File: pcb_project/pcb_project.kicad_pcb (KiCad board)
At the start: 6 copper layers, 238 parts, among them IC1 TPS54325PWPR, IC2 TPS54294PWPR, IC3 IS61WV204816BLL-10TLI, IC4 IS61WV204816BLL-10TLI, J1 Conn_01x10_Pin, J10 M20-9990246, J11 M20-9990246, J12 M20-9990246, J2 FTSH-107-01-F-DV-K, J3 Conn_ST_STDC14, J4 DE15_Socket_HighDensity_Mount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, J5 USB_B_Micro, J6 MEM2052-00-195-00-A, J7 USB_A, J8 M20-9990246, J9 M20-9990246, Q1 BC857BS, Q2 BC847BPN, SW2 SW_SPDT, SW3 SW_SPST, SW4 SW_SPST, U1 XC7A100T-FTG256, U10 TPD1E1B04DPYT, U11 TPD1E1B04DPYT, U12 TPD1E1B04DPYT, U13 TPD1E1B04DPYT, U2 STM32U595VJTx, U3 TPS2041B, U4 D3V3XA4B10LP, U5 TPD1E1B04DPYT, U6 TPD1E1B04DPYT, U7 MAX7221xWG, U8 COM-11405, U9 MT25QL128ABA1ESE-0SIT, Y1 48MHz, Y2 XLH736025.175000I

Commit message: MicroSD layout, TVS issues
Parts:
- moved R59 59.6 mm to (125.4, 62.0), turned to 45 degrees
- moved R60 59.6 mm to (123.4, 60.0), turned to 45 degrees
- moved R61 59.6 mm to (121.4, 58.0), turned to 45 degrees
- moved R62 59.6 mm to (119.4, 56.0), turned to 45 degrees
- moved R63 59.6 mm to (117.4, 54.0), turned to 45 degrees
- moved R64 59.6 mm to (115.4, 52.0), turned to 45 degrees
- moved C77 56.1 mm to (172.9, 25.7)
- moved D11 56.1 mm to (167.0, 26.2)
- moved SW3 56.1 mm to (163.8, 30.9)
- moved SW2 56.1 mm to (153.2, 23.5)
- moved U11 28.7 mm to (110.0, 38.0), turned to -45 degrees
- moved U10 25.8 mm to (112.8, 33.8), turned to -45 degrees
- moved U6 23.9 mm to (115.4, 36.6), turned to -45 degrees
- moved U5 22.3 mm to (116.4, 30.4), turned to -45 degrees
- moved U13 20.1 mm to (119.6, 33.6), turned to -45 degrees
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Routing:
- net Net-(J6-DAT0): track 1.76 -> 72.1 mm, vias 1 -> 4
- net Net-(J6-DAT1): track 1.80 -> 65.8 mm, vias 1 -> 4
- net Net-(J6-DAT2): track 13.2 -> 61.7 mm, vias 1 -> 4
- net Net-(J6-CD/DAT3): track 12.0 -> 56.2 mm, vias 1 -> 4
- net /MCU/PB4_LPGPIO1_P12: track 0.00 -> 42.0 mm
- net Net-(J6-CMD): track 11.4 -> 48.8 mm, vias 1 -> 3
- net Net-(J6-CLK): track 1.76 -> 38.9 mm, vias 1 -> 2
- net +3V3: track 17.6 -> 30.6 mm, vias 3 -> 11
- net GND: track 10.6 -> 0.01 mm
- net Net-(U2-PA13): track 0.00 -> 3.23 mm
- net /MCU/PC9_SDMMC1_D1: track 6.53 -> 5.69 mm

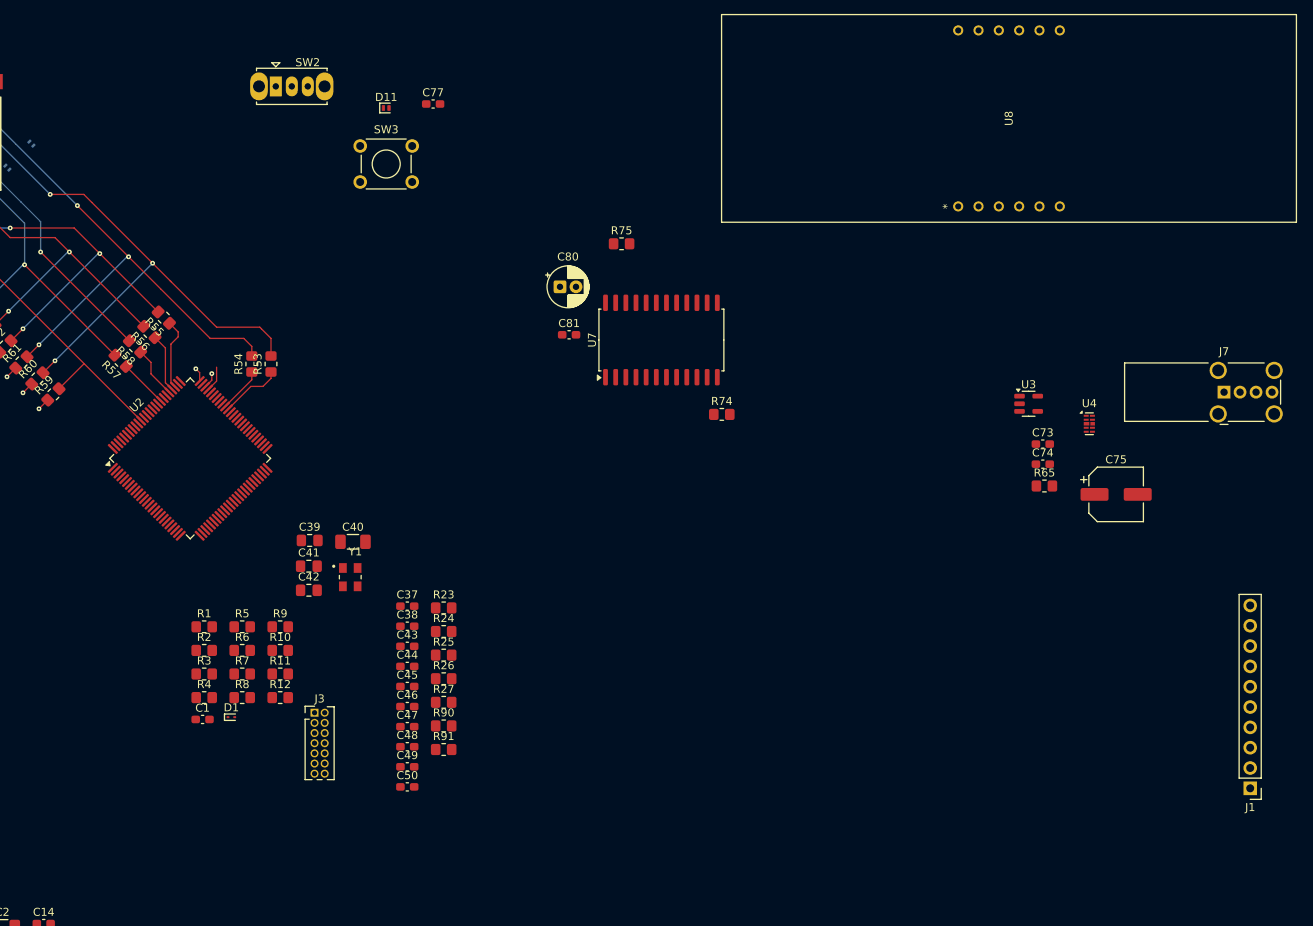
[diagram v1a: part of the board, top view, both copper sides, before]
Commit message: Layout MCU debug connector, reset and boot buttons
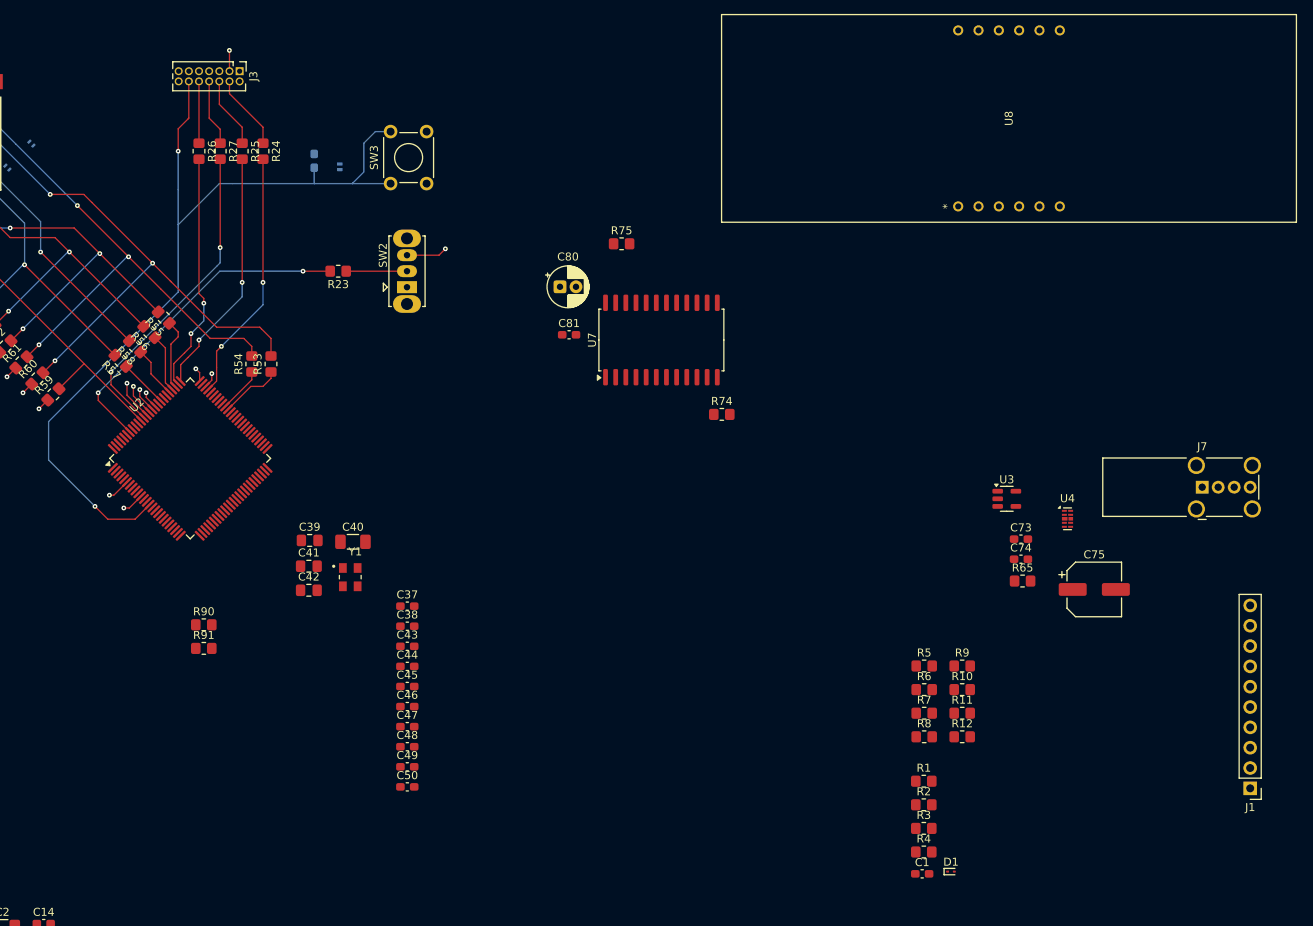
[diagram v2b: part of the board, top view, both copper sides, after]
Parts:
- C77, D11: moved to B.Cu
- moved C1 92.0 mm to (234.0, 121.9)
- moved D1 92.0 mm to (237.6, 121.7)
- moved R1 92.0 mm to (234.2, 110.3)
- moved R2 92.0 mm to (234.2, 113.3)
- moved R3 92.0 mm to (234.2, 116.2)
- moved R4 92.0 mm to (234.2, 119.2)
- moved R10 85.4 mm to (239.0, 98.9)
- moved R11 85.4 mm to (239.0, 101.8)
- moved R12 85.4 mm to (239.0, 104.8)
- moved R5 85.4 mm to (234.2, 96.0)
- moved R6 85.4 mm to (234.2, 98.9)
- moved R7 85.4 mm to (234.2, 101.8)
- moved R8 85.4 mm to (234.2, 104.8)
- moved R9 85.4 mm to (239.0, 96.0)
- moved J3 80.7 mm to (148.7, 21.6), turned to -90 degrees
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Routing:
- net Net-(D11-K): track 0.00 -> 111.3 mm, vias 0 -> 2
- net Net-(U2-PH3): track 0.00 -> 41.8 mm, vias 0 -> 2
- net Net-(U2-PB3): track 0.00 -> 39.7 mm, vias 0 -> 2
- net Net-(U2-PA14): track 0.00 -> 30.9 mm, vias 0 -> 2
- net Net-(U2-PA15): track 0.00 -> 30.1 mm, vias 0 -> 2
- net Net-(U2-PA13): track 3.23 -> 31.6 mm, vias 0 -> 2
- net +3V3: track 30.6 -> 44.0 mm, vias 11 -> 15
- net Net-(J3-JTMS/SWDIO): track 0.00 -> 9.47 mm
- net Net-(J3-JCLK/SWCLK): track 0.00 -> 8.91 mm
- net Net-(J3-JTDO/SWO): track 0.00 -> 8.30 mm
- net Net-(J3-JTDI/NC): track 0.00 -> 7.73 mm
- net Net-(SW2-B): track 0.00 -> 7.60 mm
- net /FPGA/OSPI 7: track 4.71 -> 9.70 mm, vias 0 -> 1
- net /FPGA/OSPI 6: track 2.71 -> 6.77 mm, vias 0 -> 1
- net /FPGA/OSPI 5: track 2.71 -> 5.83 mm, vias 0 -> 1
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
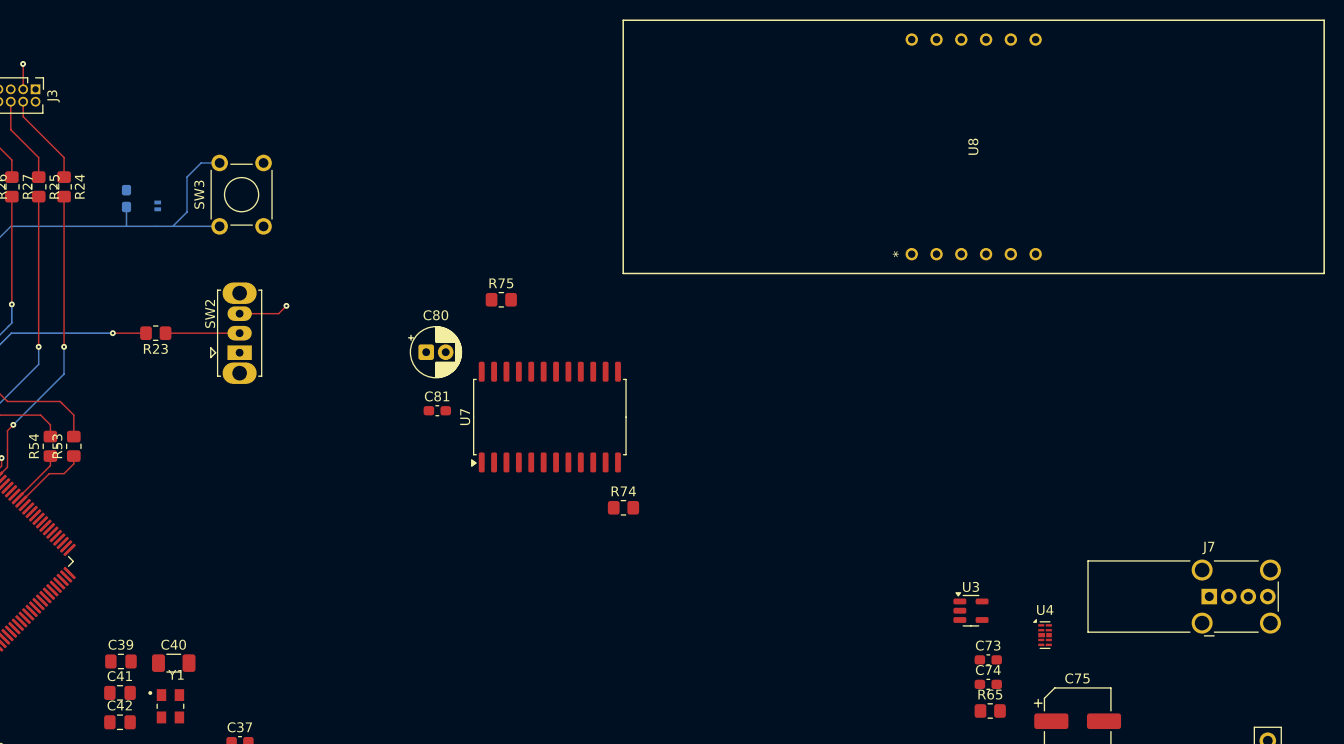
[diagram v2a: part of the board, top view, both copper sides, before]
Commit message: Led display layout
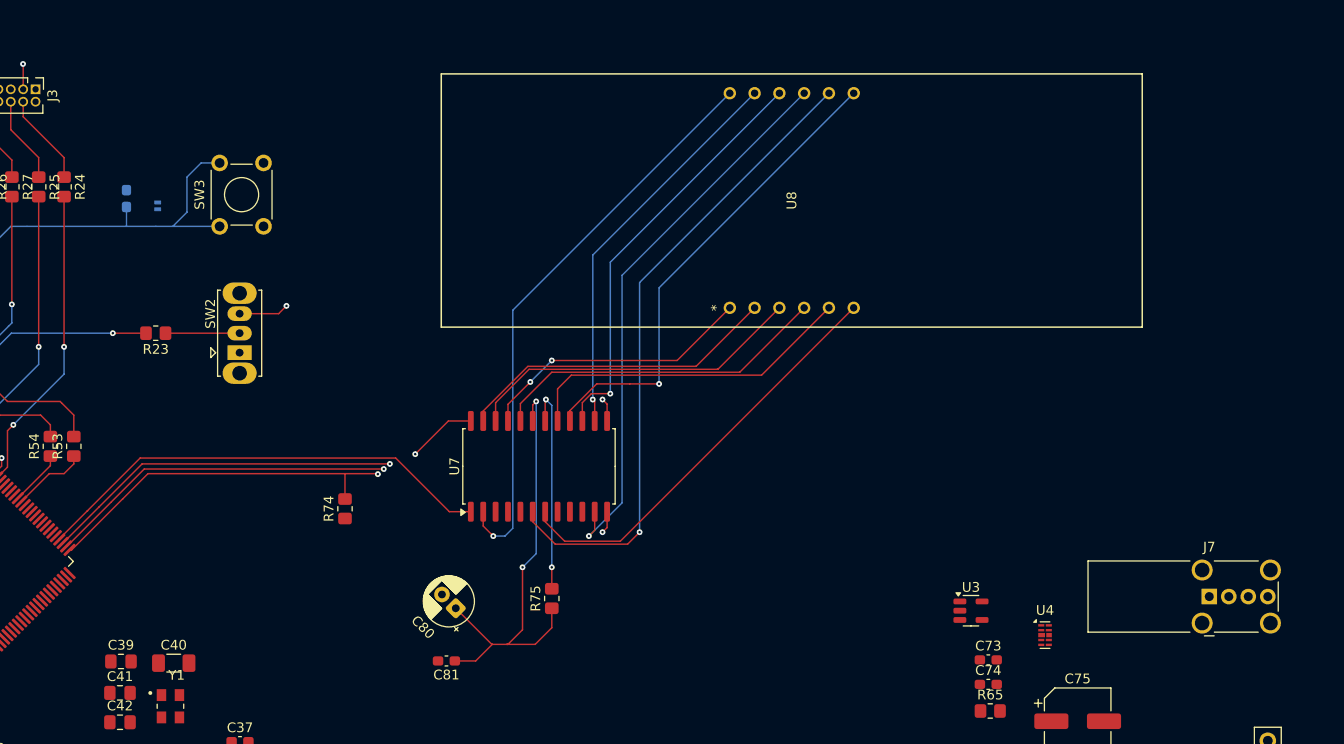
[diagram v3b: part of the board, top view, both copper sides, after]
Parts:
- moved R75 31.1 mm to (201.6, 73.8), turned to 90 degrees
- moved R74 28.6 mm to (180.4, 64.6), turned to 90 degrees
- moved C80 26.4 mm to (191.8, 74.8), turned to 135 degrees
- moved C81 25.7 mm to (190.8, 80.2), turned to 180 degrees
- moved U8 19.4 mm to (219.8, 44.0)
- moved U7 5.17 mm to (200.3, 60.2)
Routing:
- net Net-(U7-DIG_2): track 0.00 -> 66.5 mm, vias 0 -> 1
- net /7_segment_led+IC/LED_CS: track 0.00 -> 65.3 mm, vias 0 -> 2
- net /7_segment_led+IC/LED_CLK: track 0.00 -> 63.6 mm, vias 0 -> 2
- net Net-(U7-DIG_0): track 0.00 -> 59.1 mm, vias 0 -> 1
- net Net-(U7-DIG_1): track 0.00 -> 57.3 mm, vias 0 -> 1
- net /7_segment_led+IC/SEGB (7): track 0.00 -> 49.4 mm, vias 0 -> 1
- net /7_segment_led+IC/LED_MOSI: track 0.00 -> 48.0 mm
- net /7_segment_led+IC/LED_MISO: track 0.00 -> 47.0 mm, vias 0 -> 2
- net +5V: track 0.00 -> 47.0 mm, vias 0 -> 2
- net Net-(U7-DIG_3): track 0.00 -> 43.4 mm
- net /7_segment_led+IC/SEGF (10): track 0.00 -> 43.1 mm, vias 0 -> 1
- net /7_segment_led+IC/SEGA (11): track 0.00 -> 40.6 mm, vias 0 -> 1
- net Net-(U7-SEG_DP): track 0.00 -> 35.0 mm
- net /7_segment_led+IC/SEGC (4): track 0.00 -> 34.9 mm
- net /7_segment_led+IC/SEGG (5): track 0.00 -> 34.6 mm
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
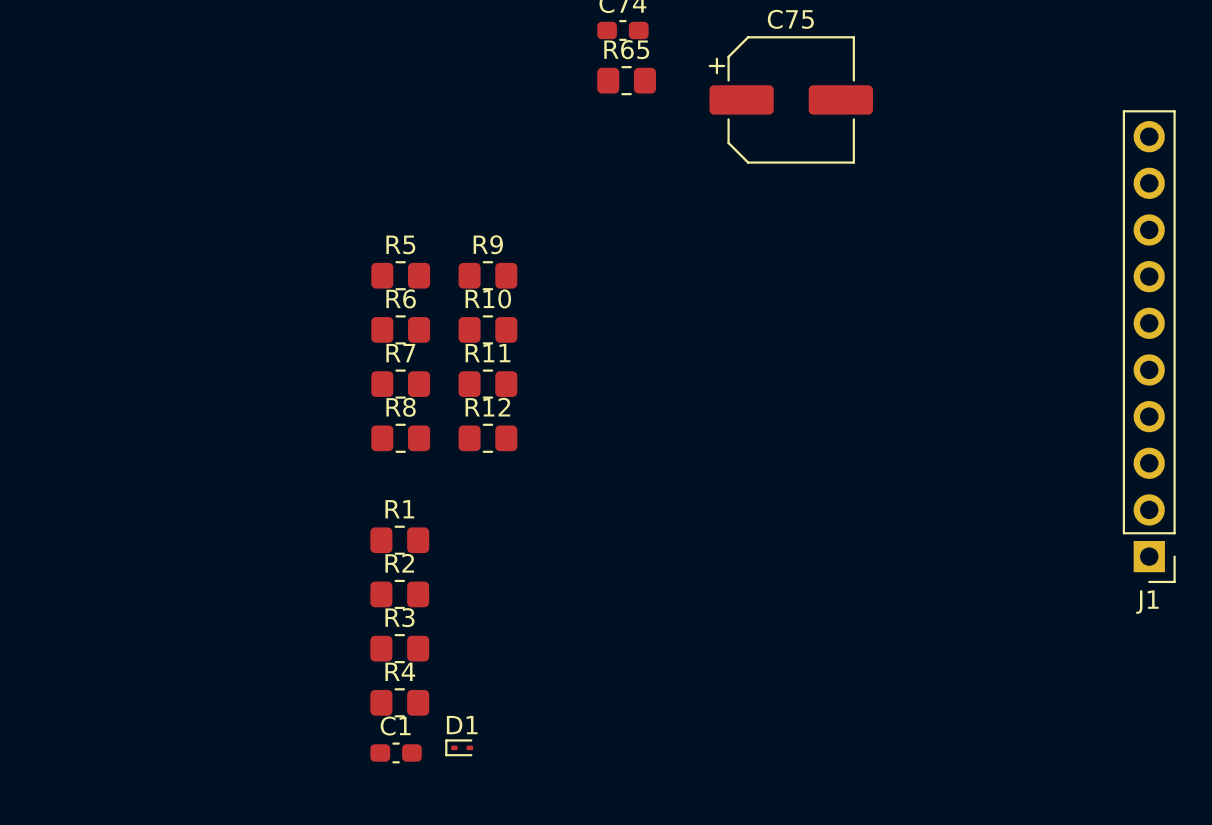
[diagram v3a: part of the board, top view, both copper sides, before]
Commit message: Update controller connector schematic
- Fix pin component so it works in layout
- Move RC filters from controller to PCB
- Remove pullups from controller as they are on pcb
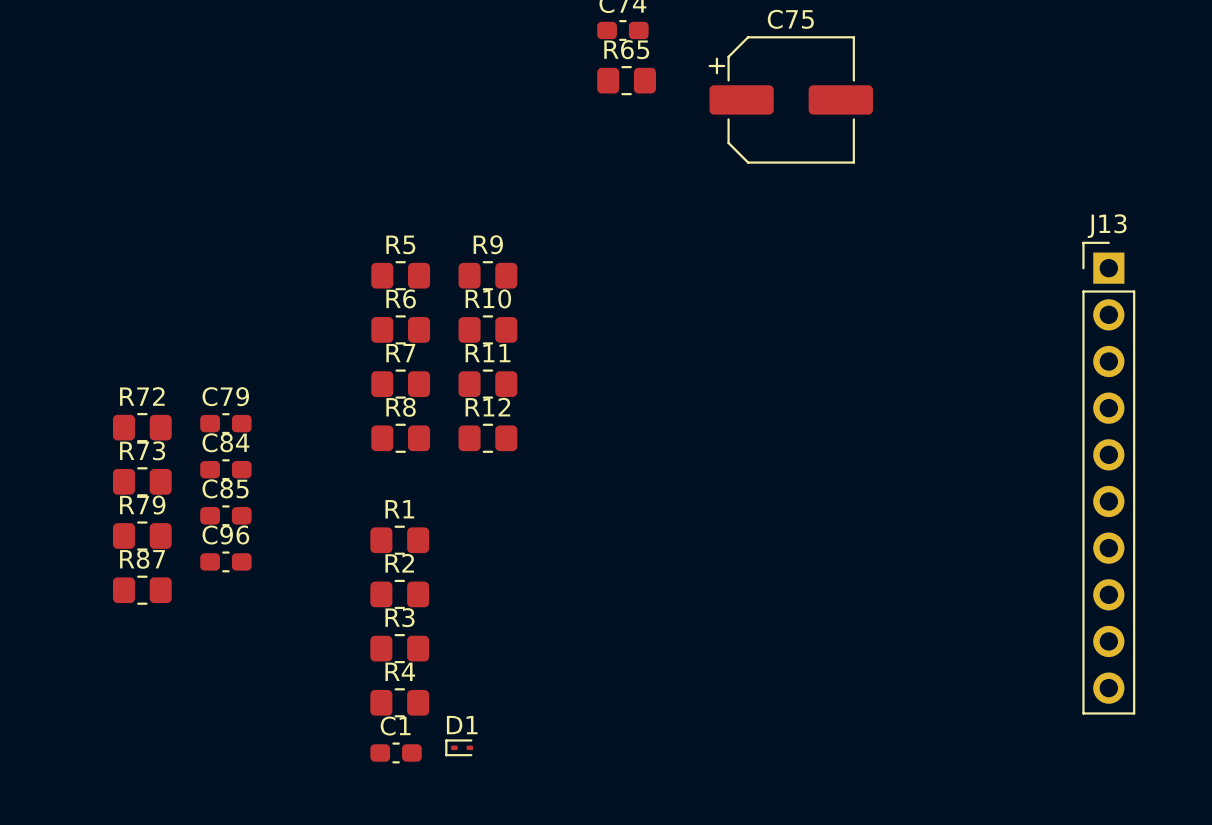
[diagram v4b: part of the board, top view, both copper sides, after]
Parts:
- removed J1: Conn_01x10_Pin, Connector_PinHeader_2.54mm:PinHeader_1x10_P2.54mm_Vertical
- added C79: 100nF, Capacitor_SMD:C_0603_1608Metric_Pad1.08x0.95mm_HandSolder, F.Cu at (224.7, 104.0)
- added C84: 100nF, Capacitor_SMD:C_0603_1608Metric_Pad1.08x0.95mm_HandSolder, F.Cu at (224.7, 106.5)
- added C85: 100nF, Capacitor_SMD:C_0603_1608Metric_Pad1.08x0.95mm_HandSolder, F.Cu at (224.7, 109.0)
- added C96: 100nF, Capacitor_SMD:C_0603_1608Metric_Pad1.08x0.95mm_HandSolder, F.Cu at (224.7, 111.5)
- added J13: Conn_01x10_Pin, Connector_PinHeader_2.54mm:PinHeader_1x10_P2.54mm_Vertical, F.Cu at (272.8, 95.5)
- added R72: 10k, Resistor_SMD:R_0805_2012Metric_Pad1.20x1.40mm_HandSolder, F.Cu at (220.2, 104.2)
- added R73: 10k, Resistor_SMD:R_0805_2012Metric_Pad1.20x1.40mm_HandSolder, F.Cu at (220.2, 107.2)
- added R79: 10k, Resistor_SMD:R_0805_2012Metric_Pad1.20x1.40mm_HandSolder, F.Cu at (220.2, 110.1)
- added R87: 10k, Resistor_SMD:R_0805_2012Metric_Pad1.20x1.40mm_HandSolder, F.Cu at (220.2, 113.1)
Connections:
- R10 pad 2: /MCU/PC2_ADC1_IN3 -> Net-(R10-Pad2)
- R11 pad 2: /MCU/PC3_ADC1_IN4 -> Net-(R11-Pad2)
- R7 pad 2: /MCU/PC0_ADC1_IN1 -> Net-(R7-Pad2)
- R8 pad 2: /MCU/PC1_ADC1_IN2 -> Net-(R73-Pad1)
